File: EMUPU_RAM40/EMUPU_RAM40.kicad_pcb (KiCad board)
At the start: 2 copper layers, 99.1 x 85.2 mm, 29 parts, among them J1 Conn_01x20_Socket, J2 Conn_01x20_Socket, J3 Barrel_Jack_Switch, J4 Conn_01x06_Pin, J5 Conn_01x08_Pin, J7 PinHeader_1x06_P2.54mm_Vertic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, SW1 SW_SPDT, SW2 SW_SPST, U1 PIC18F47Q43-IP, U2 628128

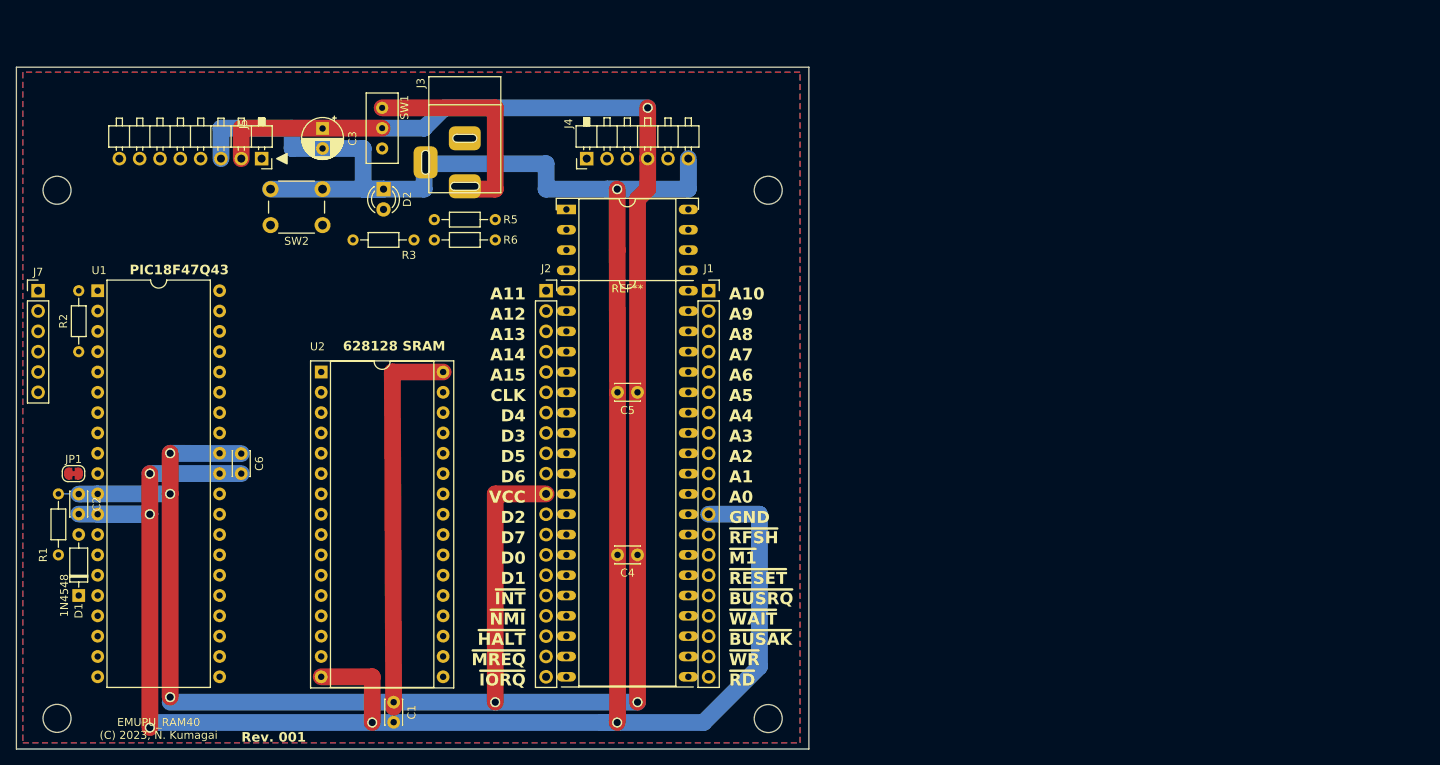
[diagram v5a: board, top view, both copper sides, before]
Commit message: Fix J4 silk, add pin names on J4, J5, fix vcc connection bottom of SRAM
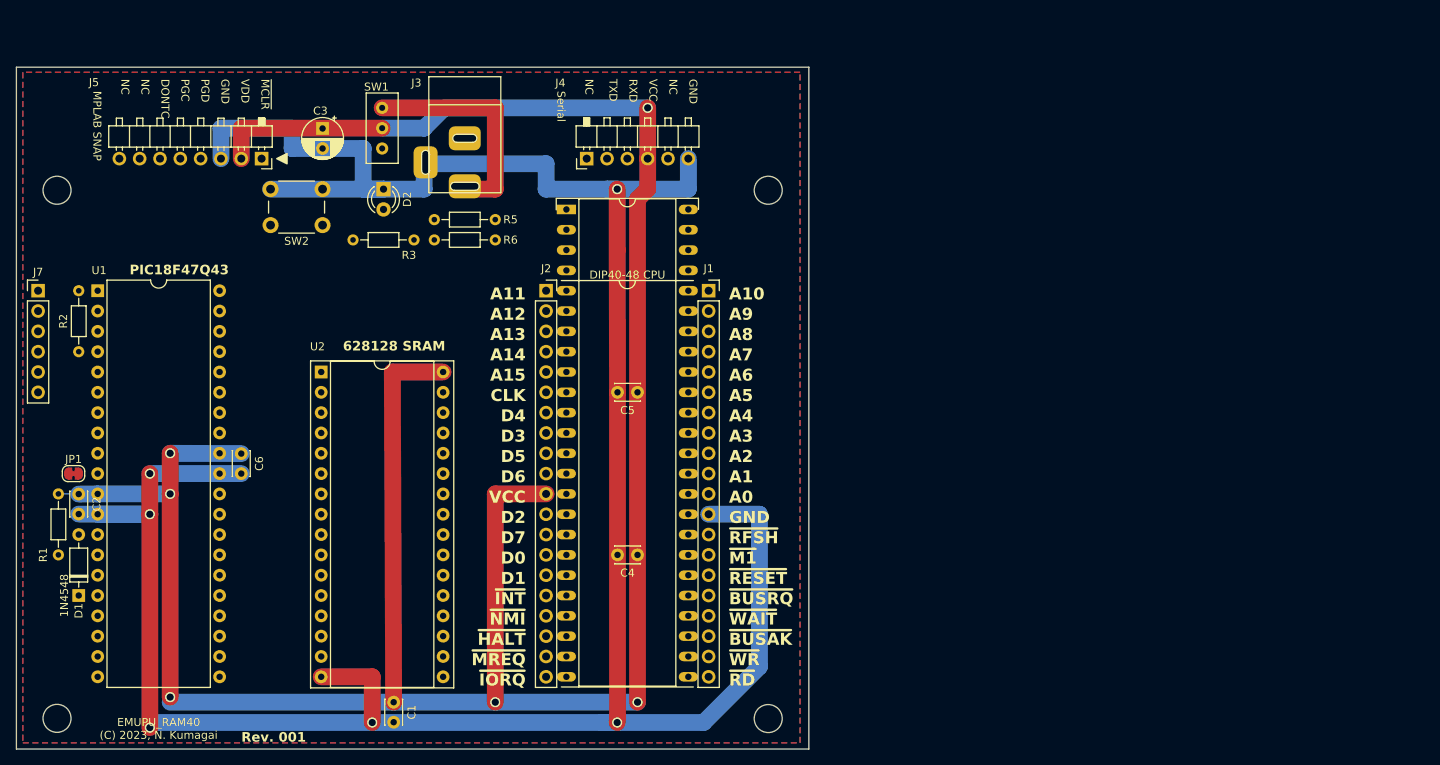
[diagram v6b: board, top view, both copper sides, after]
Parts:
- DIP40-48 CPU: renamed from REF**
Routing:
- net VCC: track 322.9 -> 322.3 mm
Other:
- board text added: "DONTC"
- board text added: "MPLAB SNAP"
- board text added: "NC"
- board text added: "PGC"
- board text added: "PGD"
- board text added: "RXD"
- board text added: "Serial"
- board text added: "TXD"
- board text added: "VDD"
- board text added: "~{MCLR}"
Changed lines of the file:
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@@
     (property "ki_keywords" "switch single-pole double-throw spdt ON-ON")
     (attr through_hole)
-    (fp_text reference "SW1" (at -2.6 -2.8 90) (layer "F.SilkS")
+    (fp_text reference "SW1" (at -5.16 0.72 -180) (layer "F.SilkS")
         (effects (font (size 1 1) (thickness 0.15)))
     )
@@
     (property "ki_keywords" "connector")
     (attr through_hole)
-    (fp_text reference "J4" (at 4.385 -2.27 90) (layer "F.SilkS")
+    (fp_text reference "J4" (at 9.47 -3.29 180) (layer "F.SilkS")
         (effects (font (size 1 1) (thickness 0.15)))
     )
@@
     (property "ki_keywords" "connector")
     (attr through_hole)
-    (fp_text reference "J5" (at 4.3446 15.576 90) (layer "F.SilkS")
+    (fp_text reference "J5" (at 9.5446 -3.109 180) (layer "F.SilkS")
         (effects (font (size 1 1) (thickness 0.15)))
     )
@@
     (property "ki_keywords" "cap capacitor")
     (attr through_hole)
-    (fp_text reference "C3" (at 1.25 -3.75 90) (layer "F.SilkS")
+    (fp_text reference "C3" (at -2.2 0.27 -180) (layer "F.SilkS")
         (effects (font (size 1 1) (thickness 0.15)))
     )
@@
     (tags "THT DIP DIL PDIP 2.54mm 15.24mm 600mil Socket LongPads")
     (attr through_hole)
-    (fp_text reference "REF**" (at 7.62 9.906) (layer "F.SilkS")
+    (fp_text reference "DIP40-48 CPU" (at 7.62 8.18) (layer "F.SilkS")
         (effects (font (size 1 1) (thickness 0.15)))
     )
@@
     (property "ki_keywords" "DC power barrel jack connector")
     (attr through_hole)
-    (fp_text reference "J3" (at -6.915 5.499 90) (layer "F.SilkS")
+    (fp_text reference "J3" (at -6.945 6.049 -180) (layer "F.SilkS")
         (effects (font (size 1 1) (thickness 0.15)))
     )
@@
     (effects (font (size 1.5 1.5) (thickness 0.3) bold) (justify right bottom))
   )
+  (gr_text "DONTC" (at 108 67.5 -90) (layer "F.SilkS")
+    (effects (font (size 1 1) (thickness 0.15)) (justify left bottom))
+  )
+  (gr_text "NC" (at 171.5 67.5 -90) (layer "F.SilkS")
+    (effects (font (size 1 1) (thickness 0.15)) (justify left bottom))
+  )
   (gr_text "A11" (at 153.67 95.25) (layer "F.SilkS")
     (effects (font (size 1.5 1.5) (thickness 0.3) bold) (justify right bottom))
@@
     (effects (font (size 1.5 1.5) (thickness 0.3) bold) (justify right bottom))
   )
+  (gr_text "NC" (at 105.5 67.5 -90) (layer "F.SilkS")
+    (effects (font (size 1 1) (thickness 0.15)) (justify left bottom))
+  )
   (gr_text "~{NMI}" (at 153.67 135.89) (layer "F.SilkS")
     (effects (font (size 1.5 1.5) (thickness 0.3) bold) (justify right bottom))
@@
     (effects (font (size 1.5 1.5) (thickness 0.3) bold) (justify left bottom))
   )
+  (gr_text "PGD" (at 113 67.5 -90) (layer "F.SilkS")
+    (effects (font (size 1 1) (thickness 0.15)) (justify left bottom))
+  )
+  (gr_text "Serial" (at 157.5 69 -90) (layer "F.SilkS")
+    (effects (font (size 1 1) (thickness 0.15)) (justify left bottom))
+  )
   (gr_text "~{BUSAK}" (at 179.07 138.43) (layer "F.SilkS")
     (effects (font (size 1.5 1.5) (thickness 0.3) bold) (justify left bottom))
@@
     (effects (font (size 1.5 1.5) (thickness 0.3) bold) (justify right bottom))
   )
+  (gr_text "GND" (at 174 67.5 -90) (layer "F.SilkS")
+    (effects (font (size 1 1) (thickness 0.15)) (justify left bottom))
+  )
   (gr_text "D0" (at 153.67 128.27) (layer "F.SilkS")
     (effects (font (size 1.5 1.5) (thickness 0.3) bold) (justify right bottom))
@@
     (effects (font (size 1.5 1.5) (thickness 0.3) bold) (justify left bottom))
   )
+  (gr_text "VCC" (at 169 67.5 -90) (layer "F.SilkS")
+    (effects (font (size 1 1) (thickness 0.15)) (justify left bottom))
+  )
   (gr_text "D5" (at 153.67 115.57) (layer "F.SilkS")
     (effects (font (size 1.5 1.5) (thickness 0.3) bold) (justify right bottom))
@@
     (effects (font (size 1.5 1.5) (thickness 0.3) bold) (justify left bottom))
   )
+  (gr_text "GND" (at 115.5 67.5 -90) (layer "F.SilkS")
+    (effects (font (size 1 1) (thickness 0.15)) (justify left bottom))
+  )
   (gr_text "A2" (at 179.07 115.57) (layer "F.SilkS")
     (effects (font (size 1.5 1.5) (thickness 0.3) bold) (justify left bottom))
@@
     (effects (font (size 1.5 1.5) (thickness 0.3) bold) (justify left bottom))
   )
+  (gr_text "MPLAB SNAP" (at 99.5 69 -90) (layer "F.SilkS")
+    (effects (font (size 1 1) (thickness 0.15)) (justify left bottom))
+  )
   (gr_text "D6" (at 153.67 118.11) (layer "F.SilkS")
     (effects (font (size 1.5 1.5) (thickness 0.3) bold) (justify right bottom))
   )
+  (gr_text "~{MCLR}" (at 120.5 67.5 -90) (layer "F.SilkS")
+    (effects (font (size 1 1) (thickness 0.15)) (justify left bottom))
+  )
+  (gr_text "TXD" (at 164 67.5 -90) (layer "F.SilkS")
+    (effects (font (size 1 1) (thickness 0.15)) (justify left bottom))
+  )
   (gr_text "~{RESET}" (at 179.07 130.81) (layer "F.SilkS")
     (effects (font (size 1.5 1.5) (thickness 0.3) bold) (justify left bottom))
@@
     (effects (font (size 1.2 1.2) (thickness 0.3) bold) (justify left bottom))
   )
+  (gr_text "PGC" (at 110.5 67.5 -90) (layer "F.SilkS")
+    (effects (font (size 1 1) (thickness 0.15)) (justify left bottom))
+  )
   (gr_text "A5" (at 179.07 107.95) (layer "F.SilkS")
     (effects (font (size 1.5 1.5) (thickness 0.3) bold) (justify left bottom))
   )
+  (gr_text "NC" (at 103 67.5 -90) (layer "F.SilkS")
+    (effects (font (size 1 1) (thickness 0.15)) (justify left bottom))
+  )
+  (gr_text "NC" (at 161 67.5 -90) (layer "F.SilkS")
+    (effects (font (size 1 1) (thickness 0.15)) (justify left bottom))
+  )
   (gr_text "CLK" (at 153.67 107.95) (layer "F.SilkS")
     (effects (font (size 1.5 1.5) (thickness 0.3) bold) (justify right bottom))
@@
     (effects (font (size 1.5 1.5) (thickness 0.3) bold) (justify right bottom))
   )
+  (gr_text "VDD" (at 118 67.5 -90) (layer "F.SilkS")
+    (effects (font (size 1 1) (thickness 0.15)) (justify left bottom))
+  )
   (gr_text "A15" (at 153.67 105.41) (layer "F.SilkS")
     (effects (font (size 1.5 1.5) (thickness 0.3) bold) (justify right bottom))
   )
+  (gr_text "RXD" (at 166.5 67.5 -90) (layer "F.SilkS")
+    (effects (font (size 1 1) (thickness 0.15)) (justify left bottom))
+  )
   (gr_text "D4" (at 153.67 110.49) (layer "F.SilkS")
     (effects (font (size 1.5 1.5) (thickness 0.3) bold) (justify right bottom))
   )
-  (segment (start 143.34 104.14) (end 136.99 104.14) (width 2.1) (layer "F.Cu") (net 1))
-  (segment (start 136.99 104.14) (end 137.16 146.05) (width 2.1) (layer "F.Cu") (net 1))
   (segment (start 168.91 71.12) (end 168.91 77.47) (width 2.1) (layer "F.Cu") (net 1))
   (segment (start 149.86 119.38) (end 149.86 145.415) (width 2.1) (layer "F.Cu") (net 1))
   (segment (start 118.11 73.66) (end 135.72 73.66) (width 2.1) (layer "F.Cu") (net 1))
+  (segment (start 143.34 104.14) (end 136.99 104.14) (width 2.1) (layer "F.Cu") (net 1))
   (segment (start 156.21 119.38) (end 149.86 119.38) (width 2.1) (layer "F.Cu") (net 1))
   (segment (start 168.91 77.47) (end 168.91 81.28) (width 2.1) (layer "F.Cu") (net 1))
@@
   (segment (start 168.91 81.28) (end 167.64 82.55) (width 2.1) (layer "F.Cu") (net 1))
   (segment (start 109.22 119.38) (end 109.22 144.78) (width 2.1) (layer "F.Cu") (net 1))
+  (segment (start 136.99 104.14) (end 137.16 145.415) (width 2.1) (layer "F.Cu") (net 1))
   (segment (start 109.22 114.3) (end 109.22 119.38) (width 2.1) (layer "F.Cu") (net 1))
   (segment (start 118.11 77.47) (end 118.11 73.66) (width 2.1) (layer "F.Cu") (net 1))
@@
       )
     )
+  )
+  (zone (net 0) (net_name "") (layers "F&B.Cu" "F.SilkS") (hatch edge 0.5)
+    (connect_pads (clearance 0))
+    (min_thickness 0.25) (filled_areas_thickness no)
+    (keepout (tracks not_allowed) (vias not_allowed) (pads not_allowed) (copperpour allowed) (footprints allowed))
+    (fill (thermal_gap 0.5) (thermal_bridge_width 0.5))
+    (polygon
+      (pts
+        (xy 90 150.5)
+        (xy 90 151.5)
+        (xy 189 151.5)
+        (xy 189 150.5)
+      )
+    )
+  )
+  (zone (net 0) (net_name "") (layers "F&B.Cu" "F.SilkS") (hatch edge 0.5)
+    (connect_pads (clearance 0))
+    (min_thickness 0.25) (filled_areas_thickness no)
+    (keepout (tracks not_allowed) (vias not_allowed) (pads not_allowed) (copperpour allowed) (footprints allowed))
+    (fill (thermal_gap 0.5) (thermal_bridge_width 0.5))
+    (polygon
+      (pts
+        (xy 188.5 66)
+        (xy 188.5 151.5)
+        (xy 189 151.5)
+        (xy 189 66)
+      )
+    )
+  )
+  (zone (net 0) (net_name "") (layers "F&B.Cu" "F.SilkS") (hatch edge 0.5)
+    (connect_pads (clearance 0))
+    (min_thickness 0.25) (filled_areas_thickness no)
+    (keepout (tracks not_allowed) (vias not_allowed) (pads not_allowed) (copperpour allowed) (footprints allowed))
+    (fill (thermal_gap 0.5) (thermal_bridge_width 0.5))
+    (polygon
+      (pts
+        (xy 90 151.5)
+        (xy 90.5 151.5)
+        (xy 90.5 66)
+        (xy 90 66)
+      )
+    )
+  )
+  (zone (net 0) (net_name "") (layers "F.Cu" "F.SilkS") (hatch edge 0.5)
+    (connect_pads (clearance 0))
+    (min_thickness 0.25) (filled_areas_thickness no)
+    (keepout (tracks not_allowed) (vias not_allowed) (pads not_allowed) (copperpour allowed) (footprints allowed))
+    (fill (thermal_gap 0.5) (thermal_bridge_width 0.5))
+    (polygon
+      (pts
+        (xy 90 66)
+        (xy 90.058338 66.518178)
+        (xy 189 66.5)
+        (xy 189 66)
+      )
+    )

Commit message: EMUPU_RAM40 PCB finished
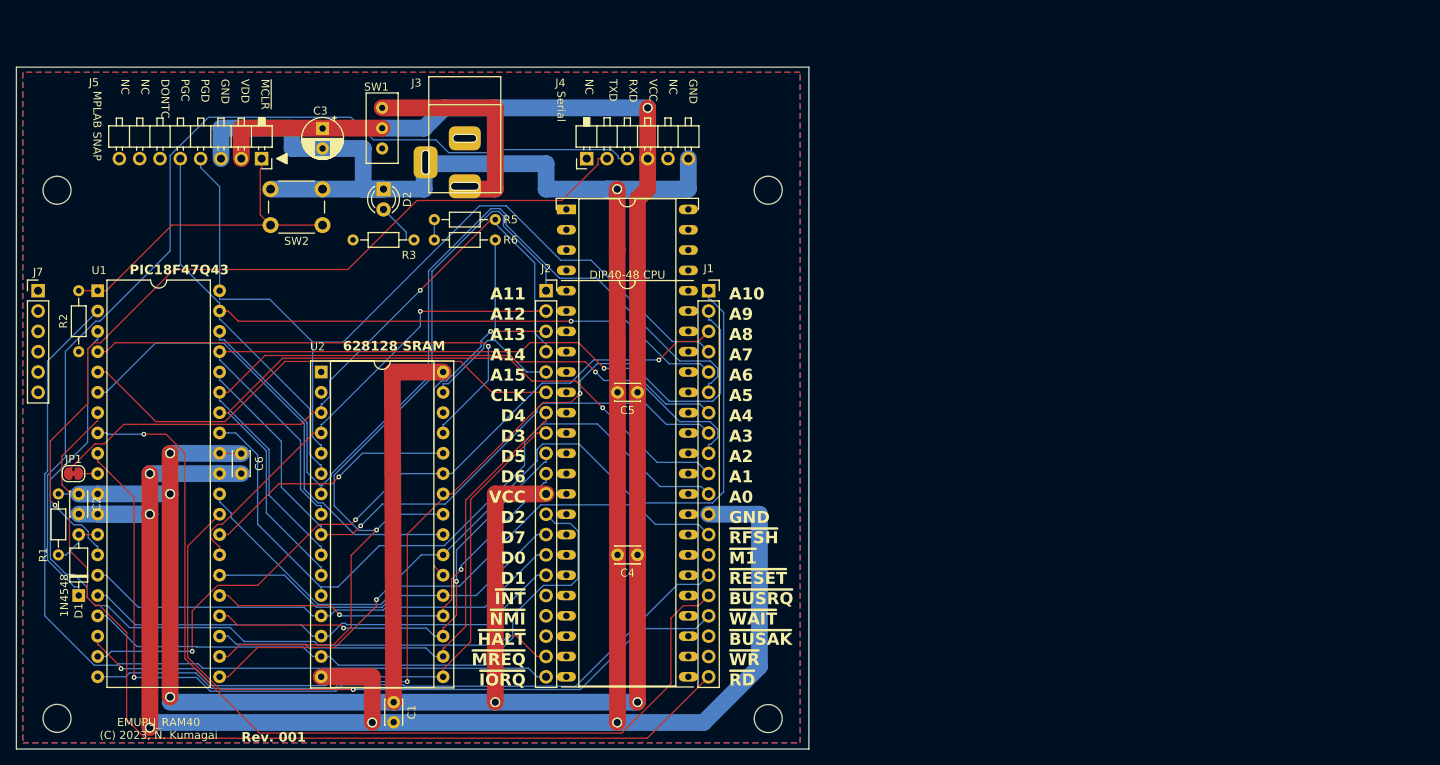
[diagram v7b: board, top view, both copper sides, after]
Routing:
- net Net-(D1-K): track 0.00 -> 125.3 mm
- net /A9: track 0.00 -> 121.4 mm, vias 0 -> 2
- net /~{RD}: track 0.00 -> 120.9 mm
- net /~{BUSRQ}: track 0.00 -> 118.9 mm, vias 0 -> 1
- net /A6: track 0.00 -> 111.2 mm, vias 0 -> 1
- net /A7: track 0.00 -> 110.9 mm
- net /A5: track 0.00 -> 110.4 mm
- net /~{RESET}: track 0.00 -> 108.7 mm, vias 0 -> 1
- net /~{IORQ}: track 0.00 -> 106.8 mm
- net /A10: track 0.00 -> 106.1 mm, vias 0 -> 1
- net Net-(J4-Pin_2): track 0.00 -> 105.9 mm, vias 0 -> 1
- net /A11: track 0.00 -> 105.3 mm, vias 0 -> 1
- net /~{MREQ}: track 0.00 -> 99.6 mm, vias 0 -> 1
- net /A2: track 0.00 -> 97.4 mm, vias 0 -> 1
- net /A1: track 0.00 -> 96.2 mm, vias 0 -> 1
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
